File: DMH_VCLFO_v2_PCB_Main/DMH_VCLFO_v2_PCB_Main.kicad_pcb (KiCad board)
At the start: 2 copper layers, 96 x 175 mm, 0 parts

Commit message: Main PCB comp placement in progress
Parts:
- added C55: 47uF, Capacitor_THT:CP_Radial_D5.0mm_P2.00mm, B.Cu at (74.1, 47.4)
- added C56: 100nF, Capacitor_THT:C_Disc_D4.3mm_W1.9mm_P5.00mm, B.Cu at (75.4, 67.6)
- added C57: 100nF, Capacitor_THT:C_Disc_D4.3mm_W1.9mm_P5.00mm, B.Cu at (75.4, 102.6)
- added C58: 100nF, Capacitor_THT:C_Disc_D4.3mm_W1.9mm_P5.00mm, B.Cu at (75.4, 137.6)
- added C59: 47uF, Capacitor_THT:CP_Radial_D5.0mm_P2.00mm, B.Cu at (125.9, 45.4)
- added C60: 100nF, Capacitor_THT:C_Disc_D4.3mm_W1.9mm_P5.00mm, B.Cu at (62.0, 72.6)
- added C61: 100nF, Capacitor_THT:C_Disc_D4.3mm_W1.9mm_P5.00mm, B.Cu at (62.0, 107.6)
- added C62: 100nF, Capacitor_THT:C_Disc_D4.3mm_W1.9mm_P5.00mm, B.Cu at (62.0, 142.6)
- added D25: SB140, Diode_THT:D_DO-41_SOD81_P10.16mm_Horizontal, B.Cu at (117.8, 44.2)
- added D26: SB140, Diode_THT:D_DO-41_SOD81_P10.16mm_Horizontal, B.Cu at (82.3, 54.4)
- added J1: TS_Jack_6.35mm_Sw, SynthStuff:CUI_MJ-63052A, F.Cu at (58.8, 171.8)
- added J10: TS_Jack_6.35mm_Sw, SynthStuff:CUI_MJ-63052A, F.Cu at (108.2, 190.2)
- added J100: IDC_02x08, SynthStuff:IDC-Header_2x08_P2.54mm_Vertical_Eurorack, B.Cu at (108.9, 48.8)
- added J11: TS_Jack_6.35mm_Sw, SynthStuff:CUI_MJ-63052A, F.Cu at (124.8, 190.2)
- added J12: TS_Jack_6.35mm_Sw, SynthStuff:CUI_MJ-63052A, F.Cu at (141.2, 190.2)
- added J13: TS_Jack_6.35mm_Sw, SynthStuff:CUI_MJ-63052A, F.Cu at (58.8, 208.8)
- added J14: TS_Jack_6.35mm_Sw, SynthStuff:CUI_MJ-63052A, F.Cu at (75.2, 208.8)
- added J15: TS_Jack_6.35mm_Sw, SynthStuff:CUI_MJ-63052A, F.Cu at (91.8, 208.8)
- added J16: TS_Jack_6.35mm_Sw, SynthStuff:CUI_MJ-63052A, F.Cu at (108.2, 208.8)
- added J17: TS_Jack_6.35mm_Sw, SynthStuff:CUI_MJ-63052A, F.Cu at (124.8, 208.8)
- added J18: TS_Jack_6.35mm_Sw, SynthStuff:CUI_MJ-63052A, F.Cu at (141.2, 208.8)
- added J2: TS_Jack_6.35mm_Sw, SynthStuff:CUI_MJ-63052A, F.Cu at (75.2, 171.8)
- added J21: IDC_02x05, SynthStuff:IDC-Header_2x05_P2.54mm_Vertical_BackBone, B.Cu at (222.8, 115.3)
- added J22: Conn_01x08, Connector_PinHeader_2.54mm:PinHeader_1x08_P2.54mm_Vertical, F.Cu at (53.0, 52.0)
- added J23: Conn_01x08, Connector_PinHeader_2.54mm:PinHeader_1x08_P2.54mm_Vertical, F.Cu at (147.0, 52.0)
- added J26: IDC_02x05, SynthStuff:IDC-Header_2x05_P2.54mm_Vertical_BackBone, B.Cu at (191.1, 115.3)
- added J27: Conn_01x08, Connector_PinHeader_2.54mm:PinHeader_1x08_P2.54mm_Vertical, F.Cu at (53.0, 94.0)
- added J28: Conn_01x08, Connector_PinHeader_2.54mm:PinHeader_1x08_P2.54mm_Vertical, F.Cu at (147.0, 94.0)
- added J3: TS_Jack_6.35mm_Sw, SynthStuff:CUI_MJ-63052A, F.Cu at (91.8, 171.8)
- added J31: IDC_02x05, SynthStuff:IDC-Header_2x05_P2.54mm_Vertical_BackBone, B.Cu at (159.3, 115.3)
- added J32: Conn_01x08, Connector_PinHeader_2.54mm:PinHeader_1x08_P2.54mm_Vertical, F.Cu at (53.0, 135.0)
- added J33: Conn_01x08, Connector_PinHeader_2.54mm:PinHeader_1x08_P2.54mm_Vertical, F.Cu at (147.0, 135.0)
- added J35: Conn_02x03_Odd_Even, Connector_PinSocket_2.54mm:PinSocket_2x03_P2.54mm_Vertical, B.Cu at (85.0, 66.0)
- added J37: Conn_02x03_Odd_Even, Connector_PinSocket_2.54mm:PinSocket_2x03_P2.54mm_Vertical, B.Cu at (85.0, 85.0)
- added J39: Conn_02x03_Odd_Even, Connector_PinSocket_2.54mm:PinSocket_2x03_P2.54mm_Vertical, B.Cu at (85.0, 145.0)
- added J4: TS_Jack_6.35mm_Sw, SynthStuff:CUI_MJ-63052A, F.Cu at (108.2, 171.8)
- added J41: Conn_02x03_Odd_Even, Connector_PinSocket_2.54mm:PinSocket_2x03_P2.54mm_Vertical, B.Cu at (105.0, 66.0)
- added J43: Conn_02x03_Odd_Even, Connector_PinSocket_2.54mm:PinSocket_2x03_P2.54mm_Vertical, B.Cu at (105.0, 85.0)
- added J45: Conn_02x03_Odd_Even, Connector_PinSocket_2.54mm:PinSocket_2x03_P2.54mm_Vertical, B.Cu at (105.0, 145.0)
- added J47: Conn_02x03_Odd_Even, Connector_PinSocket_2.54mm:PinSocket_2x03_P2.54mm_Vertical, B.Cu at (125.0, 66.0)
- added J49: Conn_02x03_Odd_Even, Connector_PinSocket_2.54mm:PinSocket_2x03_P2.54mm_Vertical, B.Cu at (125.0, 85.0)
- added J5: TS_Jack_6.35mm_Sw, SynthStuff:CUI_MJ-63052A, F.Cu at (124.8, 171.8)
- added J51: Conn_02x03_Odd_Even, Connector_PinSocket_2.54mm:PinSocket_2x03_P2.54mm_Vertical, B.Cu at (125.0, 145.0)
- added J52: Conn_01x06, Connector_PinHeader_2.54mm:PinHeader_1x06_P2.54mm_Vertical, F.Cu at (93.7, 53.9)
- added J53: Conn_01x01, Connector_PinHeader_2.54mm:PinHeader_1x01_P2.54mm_Vertical, F.Cu at (248.1, 62.4)
- added J6: TS_Jack_6.35mm_Sw, SynthStuff:CUI_MJ-63052A, F.Cu at (141.2, 171.8)
- added J7: TS_Jack_6.35mm_Sw, SynthStuff:CUI_MJ-63052A, F.Cu at (58.8, 190.2)
- added J8: TS_Jack_6.35mm_Sw, SynthStuff:CUI_MJ-63052A, F.Cu at (75.2, 190.2)
- added J9: TS_Jack_6.35mm_Sw, SynthStuff:CUI_MJ-63052A, F.Cu at (91.8, 190.2)
- added R1: 300k, Resistor_THT:R_Axial_DIN0207_L6.3mm_D2.5mm_P7.62mm_Horizontal, B.Cu at (226.5, 74.7)
- added R10: 100k, Resistor_THT:R_Axial_DIN0207_L6.3mm_D2.5mm_P7.62mm_Horizontal, B.Cu at (226.5, 103.1)
- added R17: 1k, Resistor_THT:R_Axial_DIN0207_L6.3mm_D2.5mm_P7.62mm_Horizontal, B.Cu at (226.5, 107.1)
- added R18: 300k, Resistor_THT:R_Axial_DIN0207_L6.3mm_D2.5mm_P7.62mm_Horizontal, B.Cu at (194.7, 74.7)
- added R19: 100k, Resistor_THT:R_Axial_DIN0207_L6.3mm_D2.5mm_P7.62mm_Horizontal, B.Cu at (194.7, 78.8)
- added R2: 100k, Resistor_THT:R_Axial_DIN0207_L6.3mm_D2.5mm_P7.62mm_Horizontal, B.Cu at (226.5, 78.8)
- added R20: 10M, Resistor_THT:R_Axial_DIN0207_L6.3mm_D2.5mm_P7.62mm_Horizontal, B.Cu at (194.7, 82.8)
- added R21: 100k, Resistor_THT:R_Axial_DIN0207_L6.3mm_D2.5mm_P7.62mm_Horizontal, B.Cu at (194.7, 86.9)
- added R22: 100k, Resistor_THT:R_Axial_DIN0207_L6.3mm_D2.5mm_P7.62mm_Horizontal, B.Cu at (194.7, 90.9)
- added R23: 100k, Resistor_THT:R_Axial_DIN0207_L6.3mm_D2.5mm_P7.62mm_Horizontal, B.Cu at (194.7, 95.0)
- added R25: 100k, Resistor_THT:R_Axial_DIN0207_L6.3mm_D2.5mm_P7.62mm_Horizontal, B.Cu at (194.7, 99.0)
- added R27: 100k, Resistor_THT:R_Axial_DIN0207_L6.3mm_D2.5mm_P7.62mm_Horizontal, B.Cu at (194.7, 103.1)
- added R3: 10M, Resistor_THT:R_Axial_DIN0207_L6.3mm_D2.5mm_P7.62mm_Horizontal, B.Cu at (226.5, 82.8)
- added R34: 1k, Resistor_THT:R_Axial_DIN0207_L6.3mm_D2.5mm_P7.62mm_Horizontal, B.Cu at (194.7, 107.1)
- added R35: 300k, Resistor_THT:R_Axial_DIN0207_L6.3mm_D2.5mm_P7.62mm_Horizontal, B.Cu at (163.0, 74.7)
- added R36: 100k, Resistor_THT:R_Axial_DIN0207_L6.3mm_D2.5mm_P7.62mm_Horizontal, B.Cu at (163.0, 78.8)
- added R37: 10M, Resistor_THT:R_Axial_DIN0207_L6.3mm_D2.5mm_P7.62mm_Horizontal, B.Cu at (163.0, 82.8)
- added R38: 100k, Resistor_THT:R_Axial_DIN0207_L6.3mm_D2.5mm_P7.62mm_Horizontal, B.Cu at (163.0, 86.9)
- added R39: 100k, Resistor_THT:R_Axial_DIN0207_L6.3mm_D2.5mm_P7.62mm_Horizontal, B.Cu at (163.0, 90.9)
- added R4: 100k, Resistor_THT:R_Axial_DIN0207_L6.3mm_D2.5mm_P7.62mm_Horizontal, B.Cu at (226.5, 86.9)
- added R40: 100k, Resistor_THT:R_Axial_DIN0207_L6.3mm_D2.5mm_P7.62mm_Horizontal, B.Cu at (163.0, 95.0)
- added R42: 100k, Resistor_THT:R_Axial_DIN0207_L6.3mm_D2.5mm_P7.62mm_Horizontal, B.Cu at (163.0, 99.0)
- added R44: 100k, Resistor_THT:R_Axial_DIN0207_L6.3mm_D2.5mm_P7.62mm_Horizontal, B.Cu at (163.0, 103.1)
- added R5: 100k, Resistor_THT:R_Axial_DIN0207_L6.3mm_D2.5mm_P7.62mm_Horizontal, B.Cu at (226.5, 90.9)
- added R51: 1k, Resistor_THT:R_Axial_DIN0207_L6.3mm_D2.5mm_P7.62mm_Horizontal, B.Cu at (163.0, 107.1)
- added R6: 100k, Resistor_THT:R_Axial_DIN0207_L6.3mm_D2.5mm_P7.62mm_Horizontal, B.Cu at (226.5, 95.0)
- added R8: 100k, Resistor_THT:R_Axial_DIN0207_L6.3mm_D2.5mm_P7.62mm_Horizontal, B.Cu at (226.5, 99.0)
- added U1: TL074, Package_DIP:DIP-14_W7.62mm_Socket, B.Cu at (72.5, 60.0)
- added U2: TL074, Package_DIP:DIP-14_W7.62mm_Socket, B.Cu at (72.5, 95.0)
- added U3: TL074, Package_DIP:DIP-14_W7.62mm_Socket, B.Cu at (72.5, 130.0)
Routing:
- added copper zone on B.Cu, net GND
- added copper zone on F.Cu, net GND
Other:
- board size 96 x 175 mm -> 98 x 175 mm

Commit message: Main PCB placement done
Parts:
- removed J26, J31: IDC_02x05, SynthStuff:IDC-Header_2x05_P2.54mm_Vertical_BackBone
- J53: moved to B.Cu
- moved J53 218.2 mm to (52.8, 159.7), turned to 180 degrees
- moved J21 164.7 mm to (63.5, 157.1), turned to -90 degrees
- moved R17 140.0 mm to (90.1, 138.8)
- moved R10 139.7 mm to (90.1, 133.5)
- moved R8 139.5 mm to (90.1, 128.2)
- moved R6 139.2 mm to (90.1, 123.0)
- moved R5 139.0 mm to (90.1, 117.7)
- moved R4 138.7 mm to (90.1, 112.4)
- moved R3 138.5 mm to (90.1, 107.1)
- moved R2 138.3 mm to (90.1, 101.8)
- moved R1 138.1 mm to (90.1, 96.5)
- moved R34 90.4 mm to (110.1, 138.8)
- moved R27 89.9 mm to (110.1, 133.5)
- moved R25 89.5 mm to (110.1, 128.3)
- moved R23 89.1 mm to (110.1, 123.0)
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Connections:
- J10 pad TN: /Inputs and Outputs B/Out B Saw TN -> unconnected-(J10-PadTN)
- J11 pad TN: /Inputs and Outputs B/Out B Rmp/Rnd TN -> unconnected-(J11-PadTN)
- J12 pad TN: /Inputs and Outputs B/Out B Sin/Tri TN -> B_Out_Sin_Tri_TN_M
- J14 pad TN: /Inputs and Outputs C/Sync C TN -> C_Sync_TN_M
- J15 pad TN: /Inputs and Outputs C/Out C Sqr TN -> C_Out_Sqr_TN_M
- J16 pad TN: /Inputs and Outputs C/Out C Saw TN -> unconnected-(J16-PadTN)
- J17 pad TN: /Inputs and Outputs C/Out C Rmp/Rnd TN -> unconnected-(J17-PadTN)
- J18 pad TN: /Inputs and Outputs C/Out C Sin/Tri TN -> C_Out_Sin_Tri_TN_M
- J2 pad TN: /Inputs and Outputs A/Sync A TN -> A_Sync_TN_M
- J21 pad 1: unconnected-(J21-Pin_1-Pad1) -> B_Sync_TN_M
- J21 pad 2: /Inputs and Outputs A/Sync A TN -> B_Out_Sqr_TN_M
- J21 pad 3: /Inputs and Outputs A/Out A Saw TN -> A_Sync_TN_M
- J21 pad 4: GND -> A_Out_Sqr_TN_M
- J21 pad 5: GND -> A_Out_Sin_Tri_TN_M
- J21 pad 6: /Inputs and Outputs A/Out A Rmp/Rnd TN -> C_Sync_TN_M
- J21 pad 7: /Inputs and Outputs A/Out A Sin/Tri TN -> C_Out_Sqr_TN_M
- J21 pad 8: /Inputs and Outputs A/Out A Sqr TN -> C_Out_Sin_Tri_TN_M
- J21 pad 9: GND -> B_Out_Sin_Tri_TN_M
- J3 pad TN: /Inputs and Outputs A/Out A Sqr TN -> A_Out_Sqr_TN_M
- J4 pad TN: /Inputs and Outputs A/Out A Saw TN -> unconnected-(J4-PadTN)
- J5 pad TN: /Inputs and Outputs A/Out A Rmp/Rnd TN -> unconnected-(J5-PadTN)
- J6 pad TN: /Inputs and Outputs A/Out A Sin/Tri TN -> A_Out_Sin_Tri_TN_M
- J8 pad TN: /Inputs and Outputs B/Sync B TN -> B_Sync_TN_M
- J9 pad TN: /Inputs and Outputs B/Out B Sqr TN -> B_Out_Sqr_TN_M

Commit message: Routing attempt
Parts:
- moved J37 14.0 mm to (85.0, 71.0)
- moved J43 14.0 mm to (105.0, 71.0)
- moved J49 14.0 mm to (125.0, 71.0)
- moved J35 6.00 mm to (85.0, 60.0)
- moved J41 6.00 mm to (105.0, 60.0)
- moved J47 6.00 mm to (125.0, 60.0)
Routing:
- net -12V: track 0.00 -> 132.4 mm
- net Bus_CV_M: track 0.00 -> 113.0 mm
- net +12V: track 0.00 -> 108.2 mm
- net C_VOct_Trim_p12_M: track 0.00 -> 47.1 mm
- net A_VOct_Trim_p12_M: track 0.00 -> 46.3 mm
- net B_VOct_Trim_p12_M: track 0.00 -> 43.4 mm
- net Net-(D26-A): track 0.00 -> 19.8 mm
- net Net-(D25-K): track 0.00 -> 12.3 mm
- net Net-(U3B--): track 0.00 -> 2.54 mm
- net Net-(U2D--): track 0.00 -> 2.54 mm
- net Net-(U1D--): track 0.00 -> 2.54 mm
- net Net-(U3D--): track 0.00 -> 2.54 mm
- net Net-(U2B--): track 0.00 -> 2.54 mm
- net Net-(U1B--): track 0.00 -> 2.54 mm

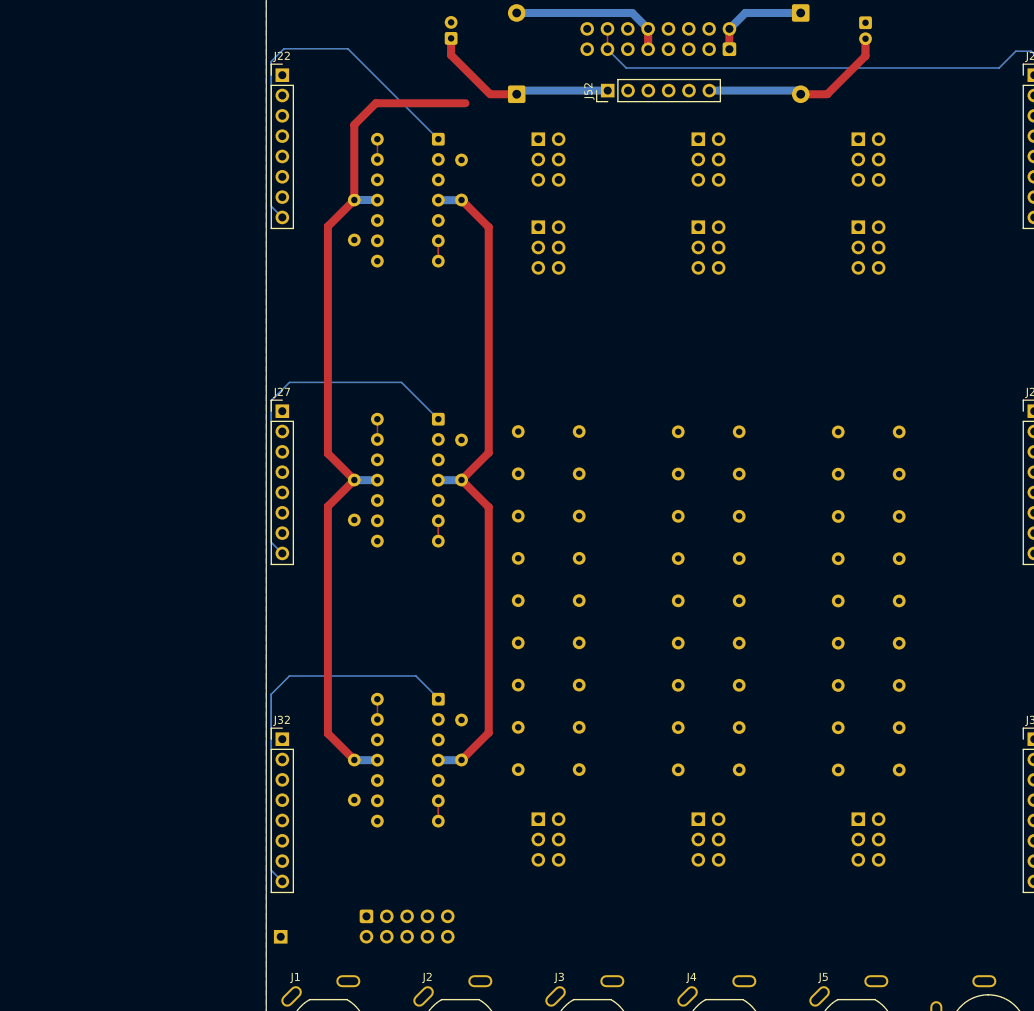
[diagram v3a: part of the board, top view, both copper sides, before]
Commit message: Alternative Main PCB placement ongoing
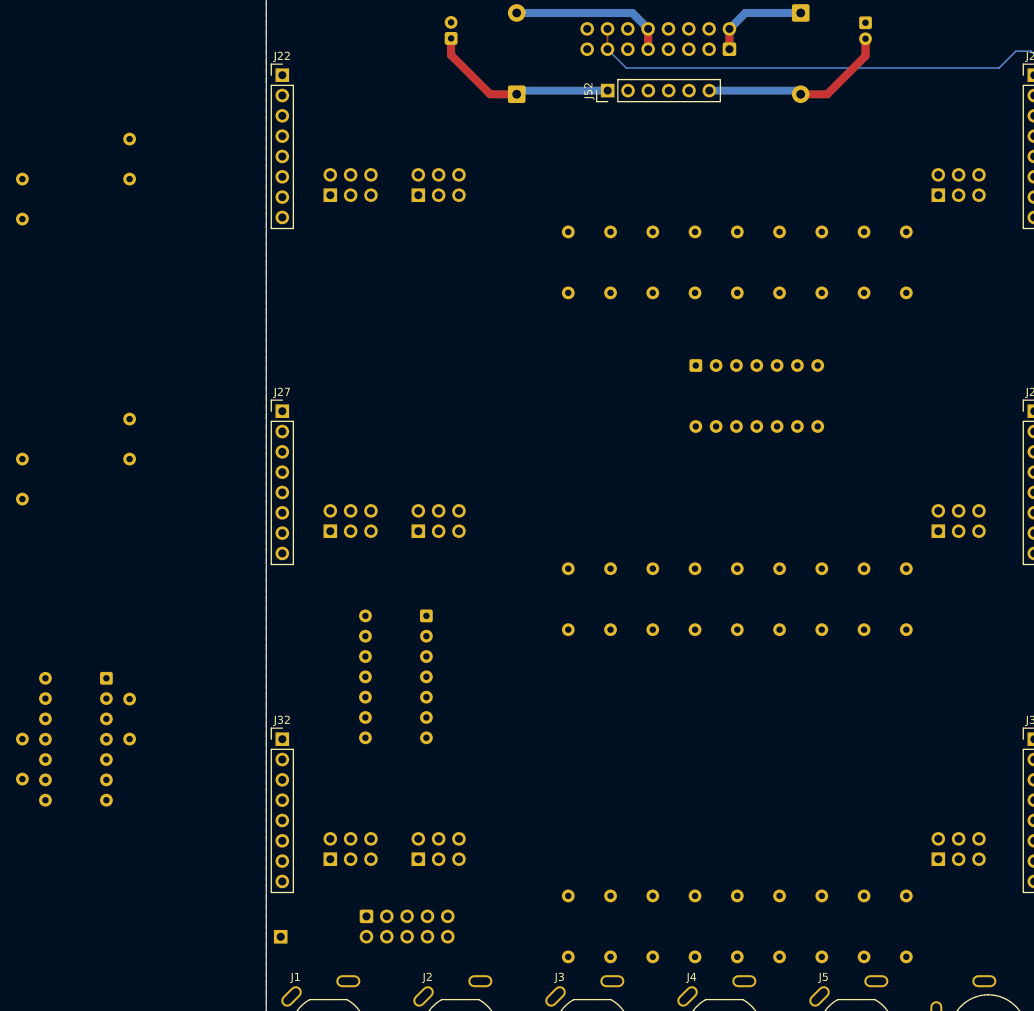
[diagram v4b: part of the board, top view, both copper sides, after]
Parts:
- moved J47 111.6 mm to (59.0, 150.0), turned to -90 degrees
- moved J49 96.3 mm to (70.0, 150.0), turned to -90 degrees
- moved J39 92.6 mm to (135.0, 67.0), turned to -90 degrees
- moved R17 78.7 mm to (131.0, 71.6), turned to -90 degrees
- moved R10 71.4 mm to (125.7, 71.6), turned to -90 degrees
- moved R35 71.2 mm to (88.7, 154.6), turned to -90 degrees
- moved J41 67.2 mm to (59.0, 109.0), turned to -90 degrees
- moved R8 64.3 mm to (120.4, 71.6), turned to -90 degrees
- moved R36 63.9 mm to (94.0, 154.6), turned to -90 degrees
- moved R6 57.1 mm to (115.2, 71.6), turned to -90 degrees
- moved R37 56.6 mm to (99.3, 154.6), turned to -90 degrees
- moved J43 51.7 mm to (70.0, 109.0), turned to -90 degrees
- moved R5 50.1 mm to (109.9, 71.6), turned to -90 degrees
- moved R38 49.3 mm to (104.6, 154.6), turned to -90 degrees
- moved J45 46.9 mm to (135.0, 109.0), turned to -90 degrees
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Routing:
- net -12V: track 132.4 -> 23.8 mm
- net +12V: track 108.2 -> 23.9 mm
- net C_VOct_Trim_p12_M: track 47.1 -> 0.00 mm
- net A_VOct_Trim_p12_M: track 46.3 -> 0.00 mm
- net B_VOct_Trim_p12_M: track 43.4 -> 0.00 mm
- net Net-(U3B--): track 2.54 -> 0.00 mm
- net Net-(U2D--): track 2.54 -> 0.00 mm
- net Net-(U1D--): track 2.54 -> 0.00 mm
- net Net-(U3D--): track 2.54 -> 0.00 mm
- net Net-(U2B--): track 2.54 -> 0.00 mm
- net Net-(U1B--): track 2.54 -> 0.00 mm

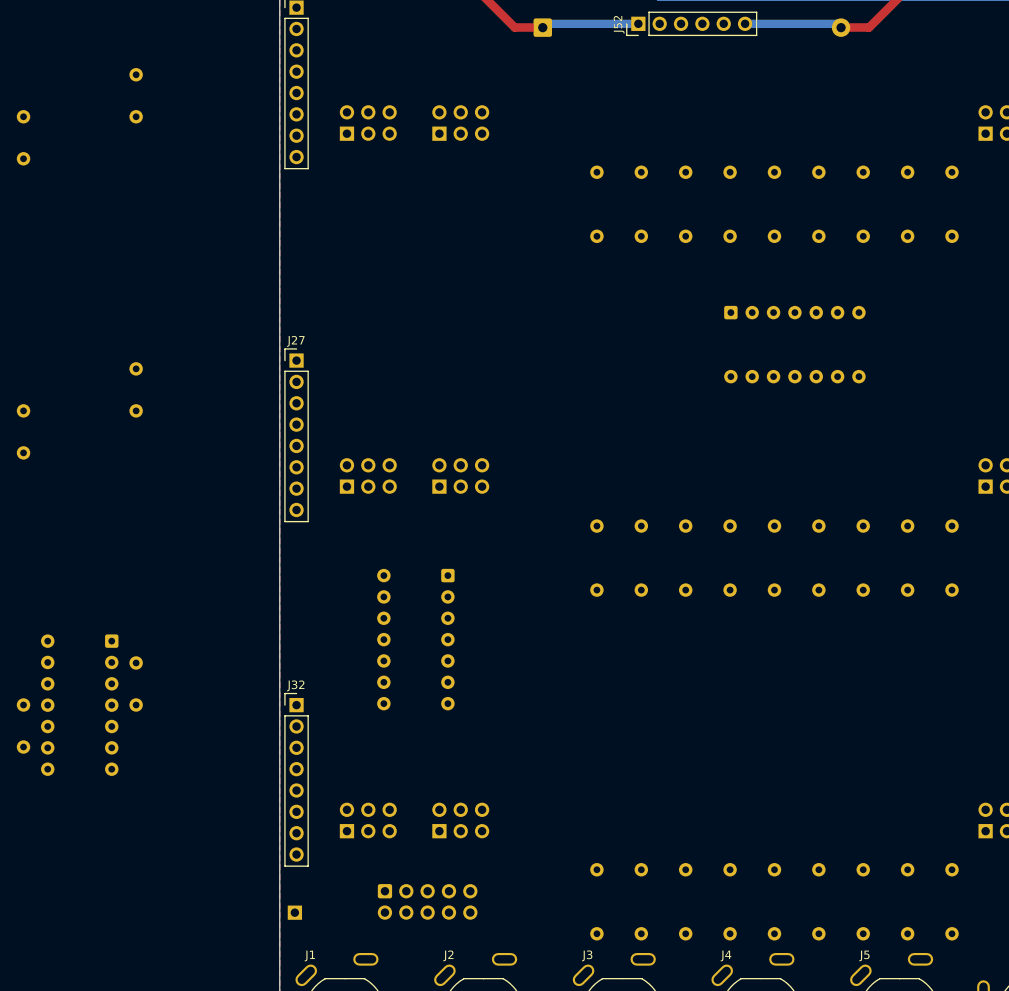
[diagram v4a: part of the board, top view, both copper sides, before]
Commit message: Placement attempt done
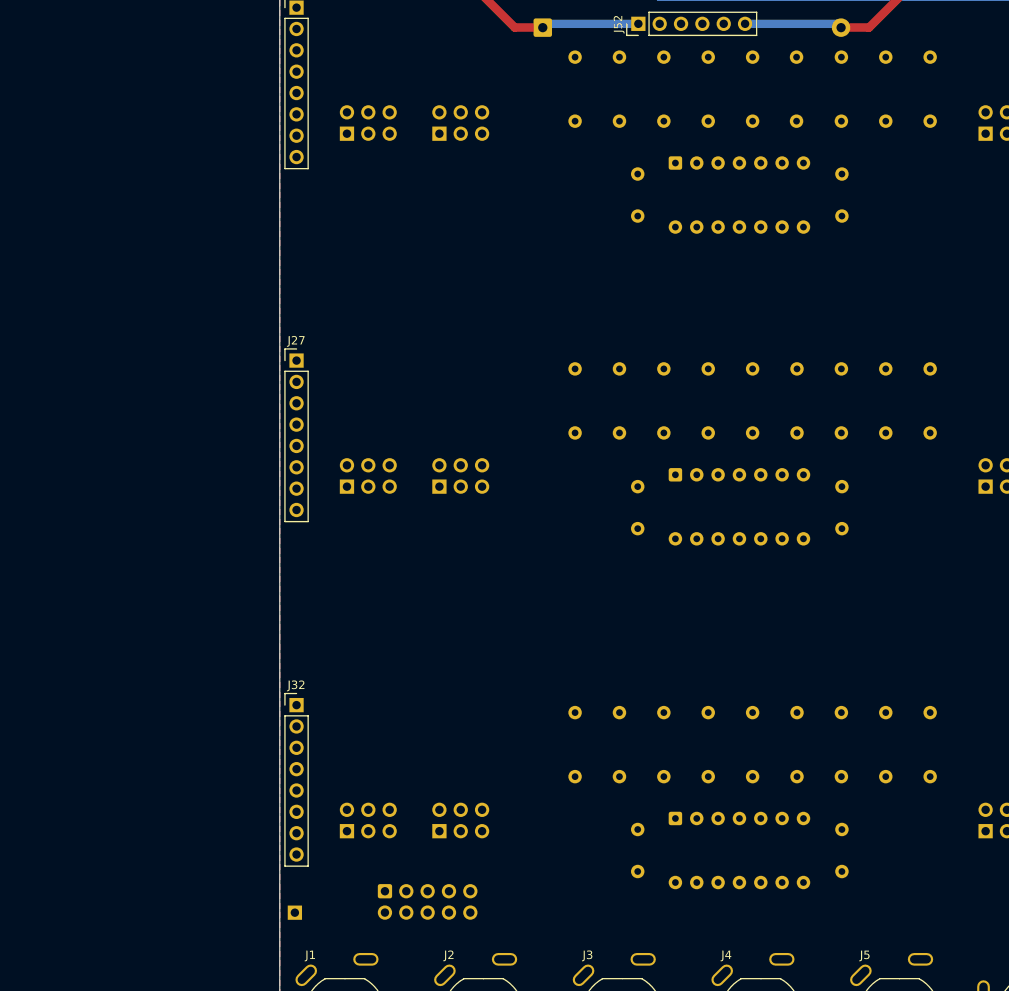
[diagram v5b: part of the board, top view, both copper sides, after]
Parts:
- moved C62 97.9 mm to (117.9, 149.8), turned to -90 degrees
- moved C61 97.5 mm to (117.9, 109.0), turned to -90 degrees
- moved C60 97.4 mm to (117.9, 71.8), turned to -90 degrees
- moved U3 70.3 mm to (98.1, 148.5), turned to -90 degrees
- moved C58 61.5 mm to (93.6, 149.8), turned to -90 degrees
- moved C57 60.4 mm to (93.6, 109.0), turned to -90 degrees
- moved C56 60.1 mm to (93.6, 71.8), turned to -90 degrees
- moved U2 29.6 mm to (98.1, 107.6), turned to -90 degrees
- moved R38 26.3 mm to (86.1, 135.9)
- moved R21 26.3 mm to (86.1, 95.0)
- moved R4 23.0 mm to (86.1, 57.9)
- moved R35 22.9 mm to (102.0, 135.9)
- moved R18 22.9 mm to (102.0, 95.0)
- moved R39 22.9 mm to (96.7, 135.9)
- moved R22 22.9 mm to (96.7, 95.0)
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
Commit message: Routing in progress
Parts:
- moved R10 7.62 mm to (117.8, 65.5), turned to 90 degrees
- moved R27 7.62 mm to (117.8, 102.6), turned to 90 degrees
- moved R44 7.62 mm to (117.8, 143.5), turned to 90 degrees
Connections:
- J37 pad 1: A_Rng_Sw_p3_M -> A_VOct_Trim_p3_M
- J37 pad 2: GND -> A_Rng_Sw_p1_M
- J37 pad 3: A_Rng_Sw_p1_M -> unconnected-(J37-Pin_3-Pad3)
- J37 pad 4: GND -> A_Rng_Sw_p3_M
- J37 pad 5: A_VOct_Trim_p3_M -> A_Sync_M
- J37 pad 6: A_Sync_M -> GND
- J39 pad 1: A_Rmp_M -> A_Sqr_M
- J39 pad 2: A_Rnd_M -> A_Rmp_M
- J39 pad 5: A_Sqr_M -> A_Tri_M
- J39 pad 6: A_Tri_M -> A_Rnd_M
- J43 pad 1: B_Rng_Sw_p3_M -> B_VOct_Trim_p3_M
- J43 pad 2: GND -> B_Rng_Sw_p1_M
- J43 pad 3: B_Rng_Sw_p1_M -> unconnected-(J43-Pin_3-Pad3)
- J43 pad 4: GND -> B_Rng_Sw_p3_M
- J43 pad 5: B_VOct_Trim_p3_M -> B_Sync_M
- J43 pad 6: B_Sync_M -> GND
- J45 pad 1: B_Rmp_M -> B_Sqr_M
- J45 pad 2: B_Rnd_M -> B_Rmp_M
- J45 pad 5: B_Sqr_M -> B_Tri_M
- J45 pad 6: B_Tri_M -> B_Rnd_M
- J49 pad 1: C_Rng_Sw_p3_M -> C_VOct_Trim_p3_M
- J49 pad 2: GND -> C_Rng_Sw_p1_M
- J49 pad 3: C_Rng_Sw_p1_M -> unconnected-(J49-Pin_3-Pad3)
- J49 pad 4: GND -> C_Rng_Sw_p3_M
- J49 pad 5: C_VOct_Trim_p3_M -> C_Sync_M
- J49 pad 6: C_Sync_M -> GND
- J51 pad 1: C_Rmp_M -> C_Sqr_M
- J51 pad 2: C_Rnd_M -> C_Rmp_M
- J51 pad 5: C_Sqr_M -> C_Tri_M
- J51 pad 6: C_Tri_M -> C_Rnd_M
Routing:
- net -12V: track 23.8 -> 358.0 mm
- net +12V: track 23.9 -> 277.3 mm
- net C_Out_Sin_Tri_TN_M: track 0.00 -> 108.7 mm
- net A_Sync_M: track 0.00 -> 107.0 mm
- net A_Sin_Tri_Sw_p2_M: track 0.00 -> 104.7 mm
- net C_FRng_Trim_p2_M: track 0.00 -> 96.8 mm
- net A_FRng_Trim_p2_M: track 0.00 -> 96.1 mm
- net B_FRng_Trim_p2_M: track 0.00 -> 95.1 mm
- net B_Sync_M: track 0.00 -> 83.5 mm
- net B_Sin_Tri_Sw_p2_M: track 0.00 -> 81.6 mm
- net B_Out_Sin_Tri_TN_M: track 0.00 -> 77.4 mm
- net C_CV_Amt_Pot_p3_M: track 0.00 -> 72.0 mm
- net B_CV_Amt_Pot_p3_M: track 0.00 -> 71.6 mm
- net A_CV_Amt_Pot_p3_M: track 0.00 -> 70.4 mm
- net A_CV_Amt_Pot_p2_M: track 0.00 -> 69.2 mm
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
